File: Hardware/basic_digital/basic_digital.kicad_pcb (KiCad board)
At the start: 4 copper layers, 90 x 55 mm, 177 parts, among them IC1 TPS65133DPDR, IC2 TPS54331DR, IC3 PCM1808PWR, J1 USB_C_Receptacle_USB2.0, J10 Conn_01x05, J11 Conn_01x03, J12 Conn_01x05, J13 Conn_01x05, J2 Conn_01x05, J3 Conn_01x03, J4 Conn_01x06, J5 Conn_01x06, J6 Conn_01x02, J7 Conn_01x05, J8 Conn_01x05, J9 Conn_01x05, Q1 MMBT4403, Q2 BC849, SW1 SW_SPST, U1 STM32F103C8Tx, U2 NE5532, U3 BQ24072RGT, U4 PCM5102, U5 NE5532, U6 NE5532, U7 ESP32-WROOM-32, U8 ESP32-WROOM-32, Y1 8Mhz

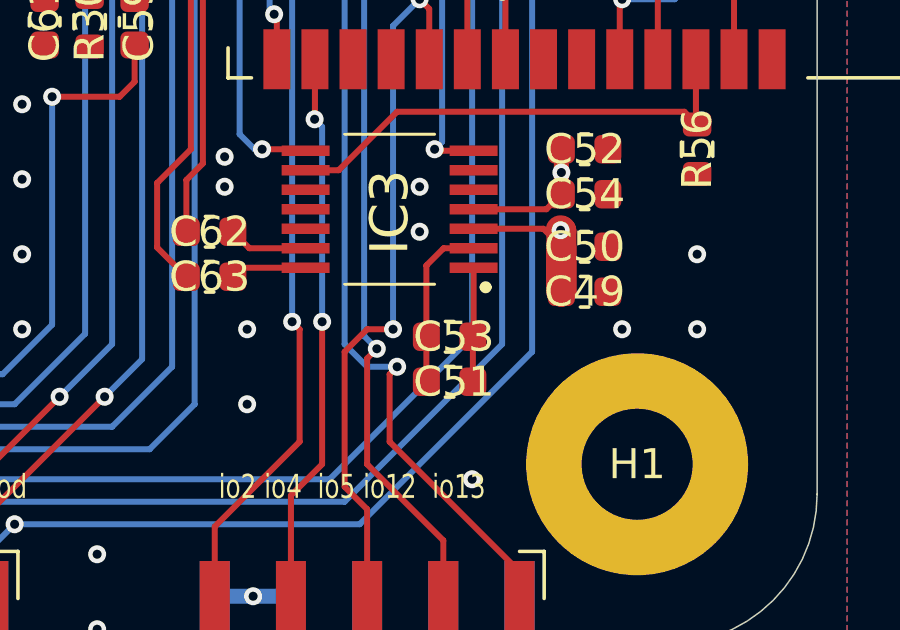
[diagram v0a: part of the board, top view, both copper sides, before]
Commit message: Mood redisign + code
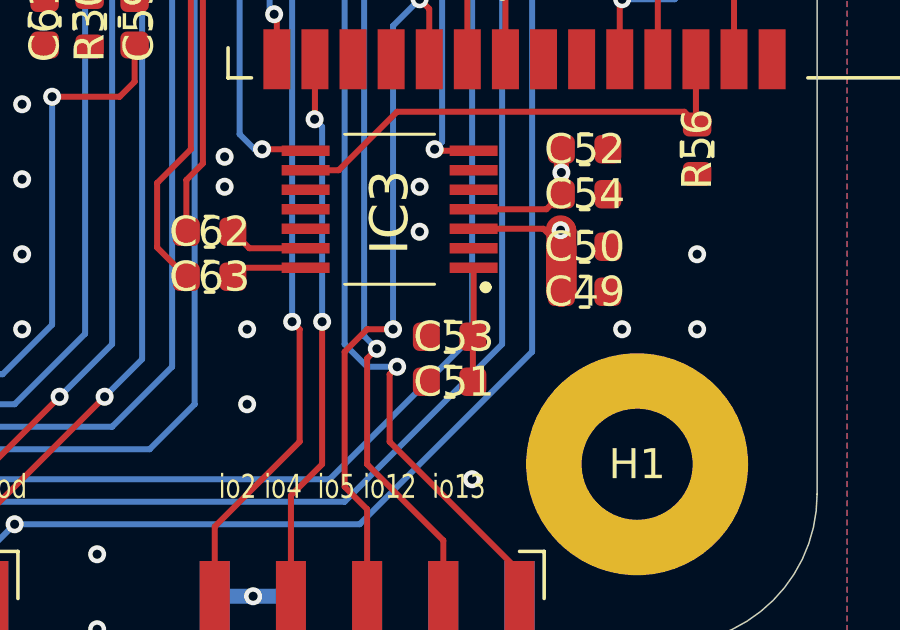
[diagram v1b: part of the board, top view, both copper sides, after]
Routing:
- net GND: track 14.4 -> 8.69 mm
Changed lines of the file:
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@@
   (segment (start 141.32548 -60.936493) (end 141.32548 -60.67452) (width 0.2) (layer "F.Cu") (net 2))
   (segment (start 148.325 -25.675) (end 149 -25) (width 0.2) (layer "F.Cu") (net 2))
-  (segment (start 181.55 -25.2) (end 182.55 -25.2) (width 0.2) (layer "F.Cu") (net 2))
   (segment (start 149.675 -24.325) (end 149 -25) (width 0.2) (layer "F.Cu") (net 2))
   (segment (start 122.6125 -18.8375) (end 122.475 -18.7) (width 0.2) (layer "F.Cu") (net 2))
   (segment (start 143.286587 -60.69952) (end 142.69952 -60.69952) (width 0.2) (layer "F.Cu") (net 2))
-  (segment (start 180.975 -24.625) (end 181.55 -25.2) (width 0.2) (layer "F.Cu") (net 2))
   (segment (start 141.25 -61.011973) (end 141.32548 -60.936493) (width 0.2) (layer "F.Cu") (net 2))
   (segment (start 141.32548 -60.67452) (end 142 -60) (width 0.2) (layer "F.Cu") (net 2))
-  (segment (start 180.975 -20.75) (end 180.975 -22.25) (width 0.2) (layer "F.Cu") (net 2))
   (segment (start 150.45 -24.325) (end 149.675 -24.325) (width 0.2) (layer "F.Cu") (net 2))
   (segment (start 142.25 -61.4375) (end 142.25 -60.25) (width 0.2) (layer "F.Cu") (net 2))
@@
   (segment (start 143.337067 -60.75) (end 143.286587 -60.69952) (width 0.2) (layer "F.Cu") (net 2))
   (segment (start 142.69952 -60.69952) (end 142 -60) (width 0.2) (layer "F.Cu") (net 2))
-  (segment (start 180.975 -22.25) (end 180.975 -24.625) (width 0.2) (layer "F.Cu") (net 2))
   (segment (start 143.4375 -60.75) (end 143.337067 -60.75) (width 0.2) (layer "F.Cu") (net 2))
   (segment (start 142.25 -60.25) (end 142 -60) (width 0.2) (layer "F.Cu") (net 2))
